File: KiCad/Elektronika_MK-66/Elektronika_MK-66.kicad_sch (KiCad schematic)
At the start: 58 parts, among them SW1 C, SW10 )], SW11 4, SW12 5, SW13 6, SW14 =, SW15 <->, SW16 1, SW17 2, SW18 3, SW19 X, SW2 ВП, SW20 ÷, SW21 0, SW22 ., SW23 π, SW24 +, SW25 -, SW26 Г Р, SW27 POWER, SW3 /-/, SW4 F, SW5 arc, SW6 7, SW7 8, SW8 9, SW9 [(, U1 К145ИП15, U2 ПН-1

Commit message: Work in progress
Original schematic redrawn, needs to be verified against actual board due to unclear "smudges" on original schematic.
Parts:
- added U3: ИЛЦ2-12/8Л, symbol Clueless_Engineer:ILC2-12/8L
- added VD1: D, symbol Device:D
- R1: value R -> Not fitted?
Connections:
- net at R21.1, SW12.1, SW17.1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: now also U3.7
- net at R24.1, SW10.1, SW15.1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: now also U3.4
- net at R17.1, U1.37: now also U3.10
- net at R15.2, R16.2, R17.2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: now also R1.2, R10.1, R11.1, R2.1, R3.1, R4.1, R5.1, R6.1, R7.1, R8.1, R9.1, U2.3
- net at R10.2, U1.40: now also SW26.1 (A)
- net at R22.1, SW13.1, SW18.1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: now also U3.6
- net at R8.2, U1.20: now also U3.18
- net at R6.2, U1.22: now also U3.21
- net at R18.1, U1.36: now also U3.1
- net at R3.2, U1.25: now also U3.16
- net at R20.1, SW1.1, SW11.1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: now also U3.8
- net at R26.1, U1.27: now also U3.9
- net at R9.2, U1.19: now also U3.17
- net at R23.1, SW14.1, SW19.1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: now also U3.5
- net at R5.2, U1.23: now also U3.13
- net at C2.1, SW27.1 (A), U1.1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: now also C1.1, U1.32, U2.2, VD1.1 (K)
- net at R7.2, U1.21: now also U3.20
- net at R4.2, U1.24: now also U3.19
- net at R2.2, U1.26: now also U3.14
- net at R25.1, U1.34: now also U3.3
- net at R19.1, U1.35: now also U3.2
- net at R16.1, U1.38: now also U3.12
- net at R15.1, U1.39: now also U3.11
- net at U2.4: now also U3.22
- net at U2.5: now also R1.1, U3.15
- net at R12.1: now also R11.2, VD1.2 (A)
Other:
- moved on the sheet: BT1, C1, C2, R1, R10, R11, R12, R13, R14, R15, R16, R17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

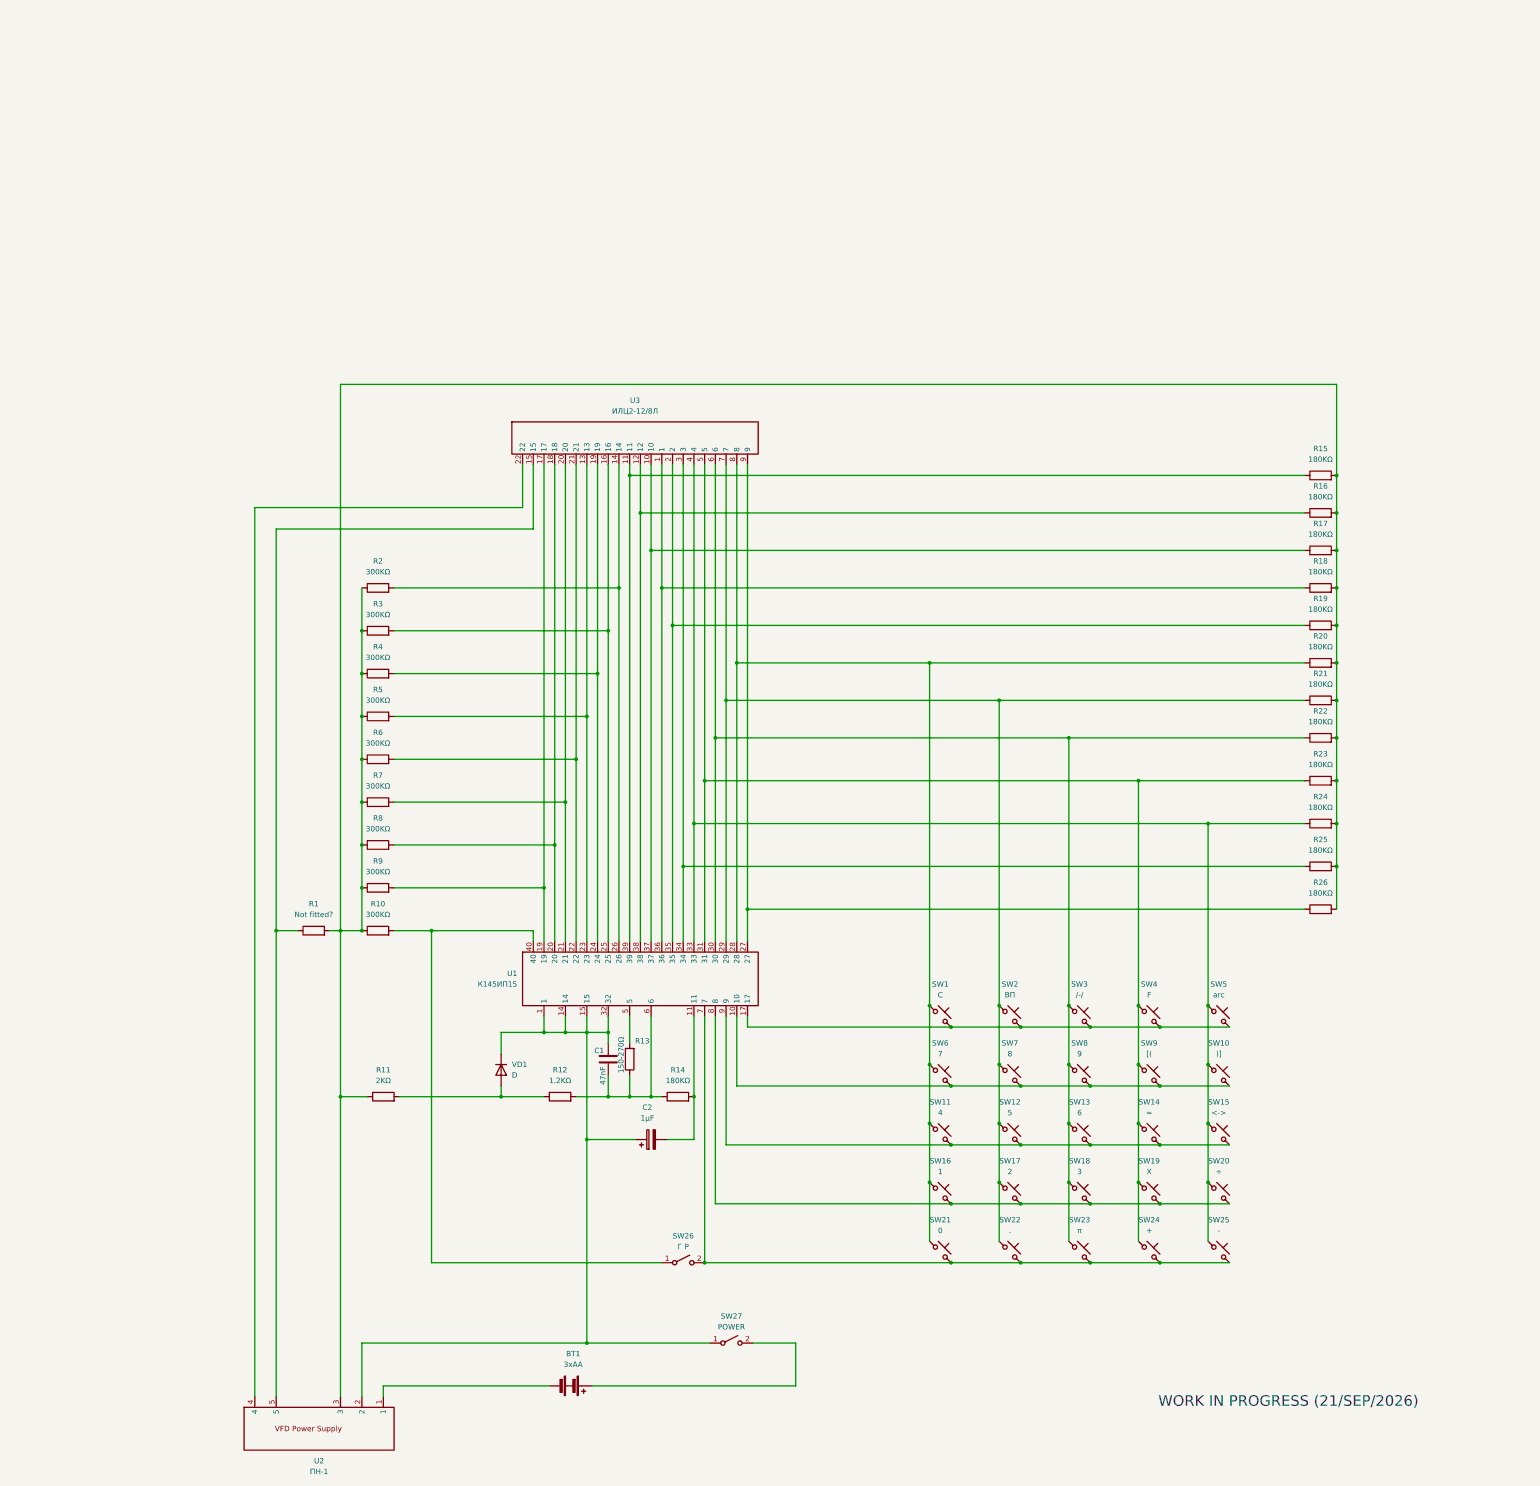
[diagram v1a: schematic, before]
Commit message: Updating schematic
I don't trust the MK-66 schema from the manual which lists a К145ИП15 ... working it out from the physical PCB with К145ИП16Б
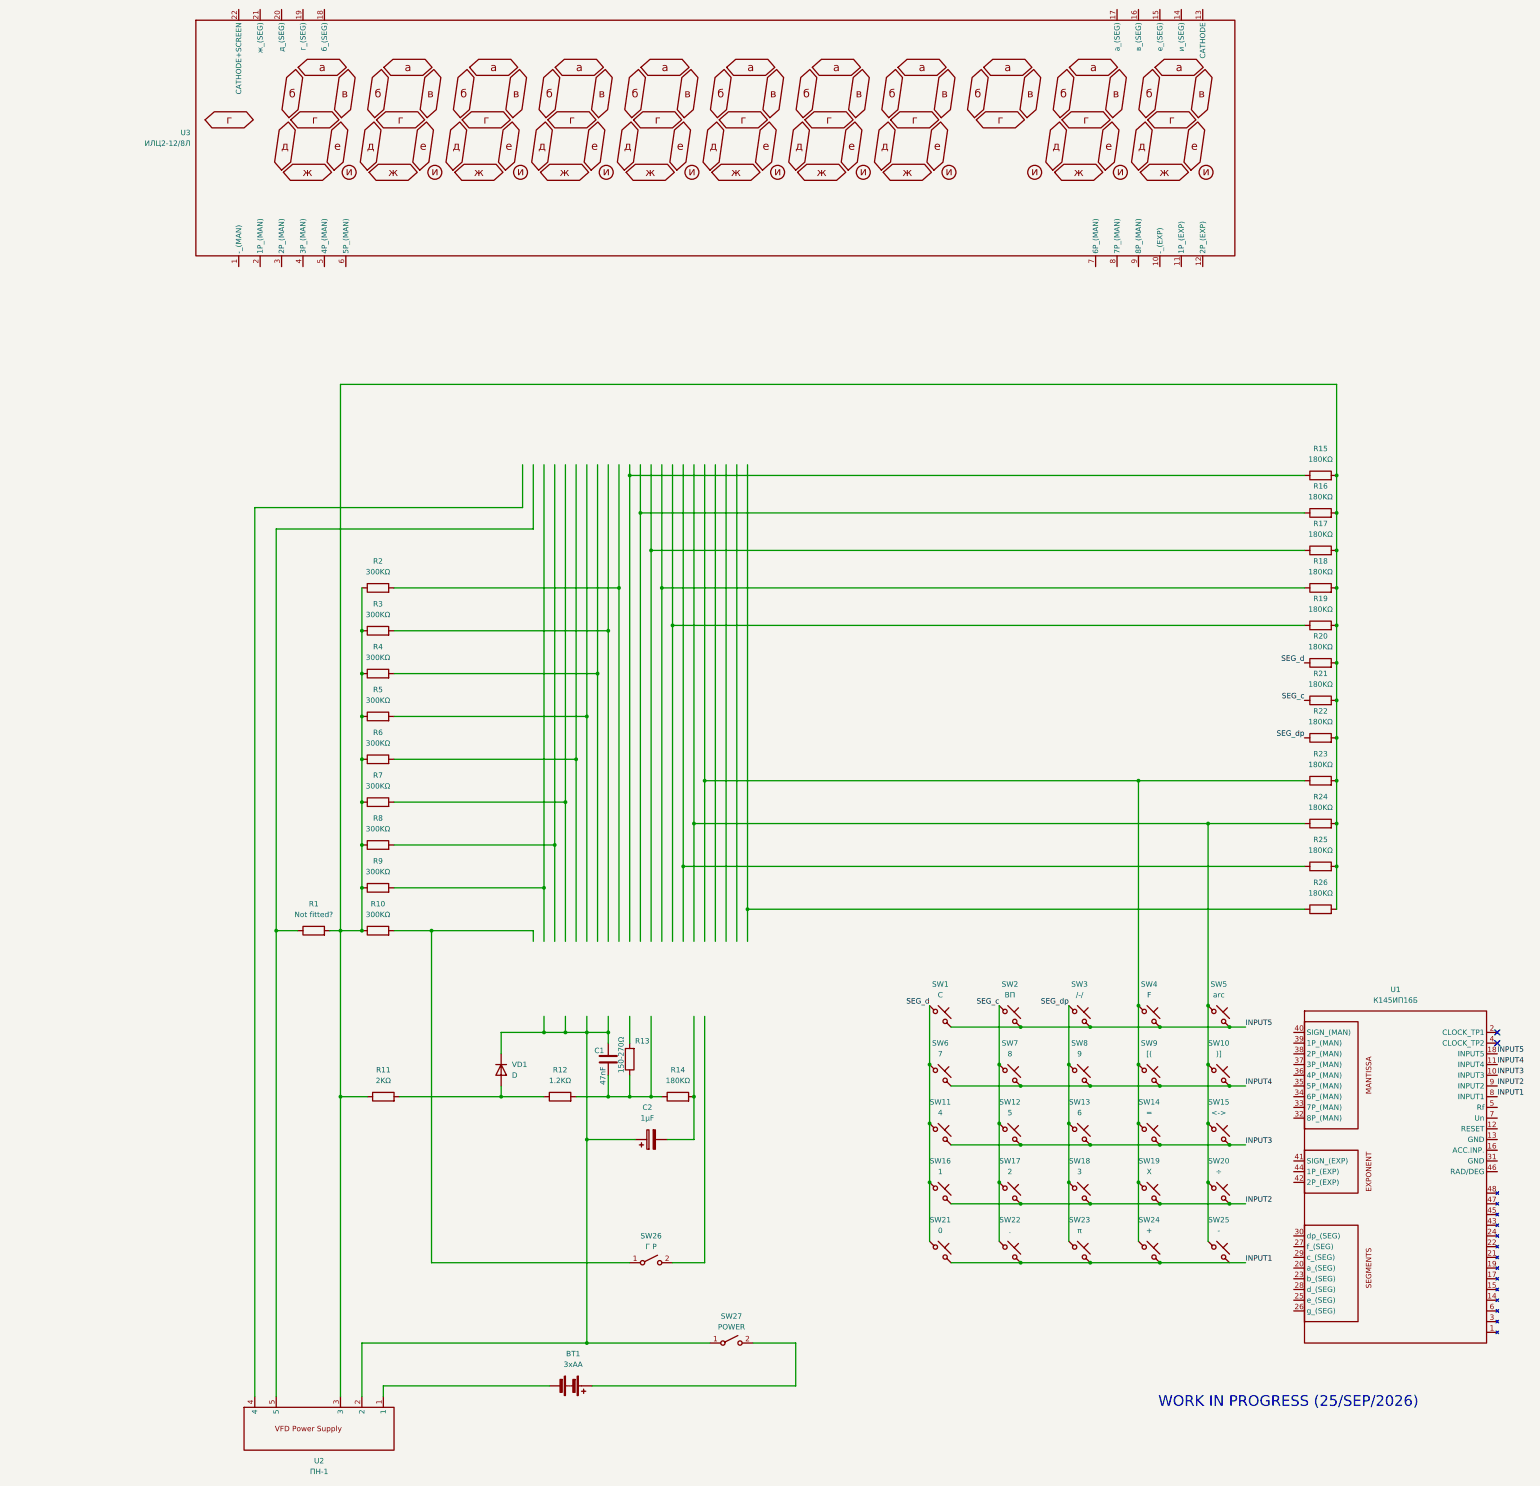
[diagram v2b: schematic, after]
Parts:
- removed U1: К145ИП15, symbol Clueless_Engineer:K145IP15
- added U1: К145ИП16Б, symbol Clueless_Engineer:K145IP16B
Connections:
- net SEG_c: now reaches R21.1, SW12.1, SW17.1, SW2.1, SW22.1, SW7.1
- net SEG_c: no longer U3.7
- net INPUT4: now reaches SW10.2, SW6.2, SW7.2, SW8.2, SW9.2
- net INPUT4: now also U1.11 (INPUT4)
- net at R24.1, SW10.1, SW15.1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: no longer U3.4
- net INPUT5: now reaches SW1.2, SW2.2, SW3.2, SW4.2, SW5.2
- net INPUT5: now also U1.18 (INPUT5)
- net at R17.1: no longer U3.10
- net SEG_dp: now reaches R22.1, SW13.1, SW18.1, SW23.1, SW3.1, SW8.1
- net SEG_dp: no longer U3.6
- net INPUT1: now reaches SW21.2, SW22.2, SW23.2, SW24.2
- net INPUT1: now also U1.8 (INPUT1); no longer SW25.2, SW26.2 (B)
- net at R8.2: no longer U3.18
- net at R6.2: no longer U3.21
- net at R18.1: no longer U3.1
- net at R3.2: no longer U3.16
- net SEG_d: now reaches R20.1, SW1.1, SW11.1, SW16.1, SW21.1, SW6.1
- net SEG_d: no longer U3.8
- net INPUT3: now reaches SW11.2, SW12.2, SW13.2, SW14.2, SW15.2
- net INPUT3: now also U1.10 (INPUT3)
- net at R26.1: no longer U3.9
- net at R9.2: no longer U3.17
- net INPUT2: now reaches SW16.2, SW17.2, SW18.2, SW19.2, SW20.2
- net INPUT2: now also U1.9 (INPUT2)
- net at R23.1, SW14.1, SW19.1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: no longer U3.5
- net at R5.2: no longer U3.13
- net at R15.1: no longer U3.11
- net at R16.1: no longer U3.12
- net at R2.2: no longer U3.14
- net at R1.1, U2.5: no longer U3.15
- net at R4.2: no longer U3.19
- net at R19.1: no longer U3.2
- net at R7.2: no longer U3.20
- net at U2.4: no longer U3.22
- net at R25.1: no longer U3.3
- no-connect marks 0 -> 2
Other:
- note added: "WORK IN PROGRESS (25/SEP/2026)"
- note removed: "WORK IN PROGRESS (21/SEP/2026)"
- moved on the sheet: SW26
